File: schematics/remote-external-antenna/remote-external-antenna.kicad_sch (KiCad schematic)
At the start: 0 parts

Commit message: Added eeprom wiring to schematic
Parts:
- added R1, R2: R, symbol Device:R
- added U1: XIAO-ESP32-C6-SMD, Seeed_Studio_XIAO_Series:XIAO-ESP32-C6-SMD, symbol Seeed_Studio_XIAO_Series:XIAO-ESP32-C6-SMD
- added U2: 24LC1025, Package_SO:SOIC-8_3.9x4.9mm_P1.27mm, symbol Memory_EEPROM:24LC1025
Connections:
- new net: R2.2, U1.5 (D4), U2.5 (SDA)
- new net: R1.2, U1.6 (D5), U2.6 (SCL)
- new net +3V3: R1.1, R2.1, U1.12 (3V3_OUT), U2.1 (A0), U2.2 (A1), U2.3 (A2), U2.8 (VCC)
- new net GND: U1.13 (GND), U2.4 (GND), U2.7 (WP)
- no-connect marks 0 -> 11

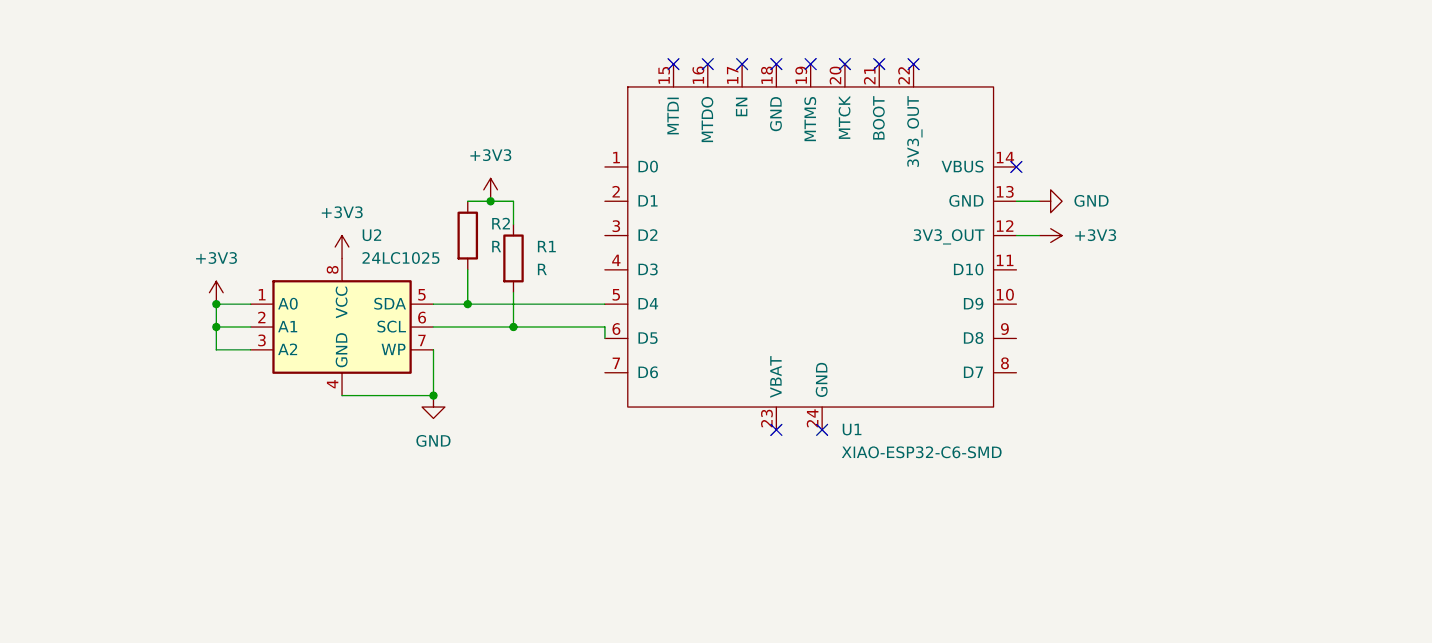
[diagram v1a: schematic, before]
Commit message: expanded schematic with led button and cc1101 module
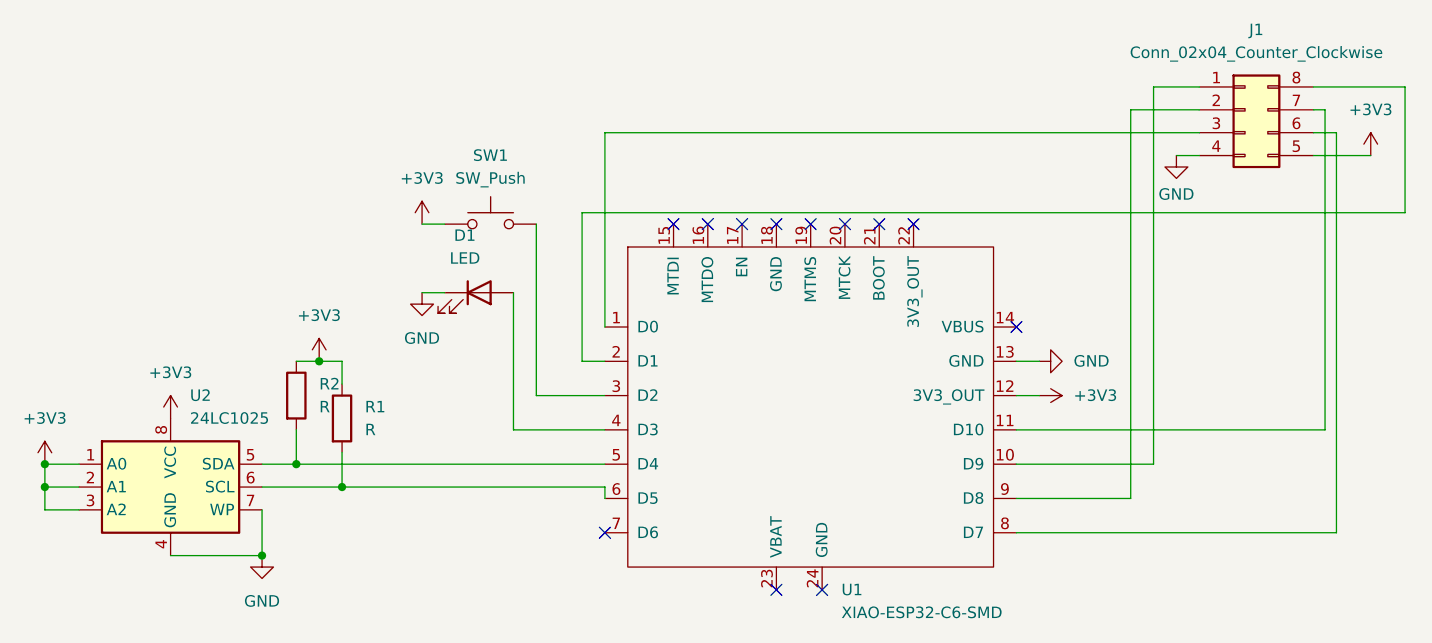
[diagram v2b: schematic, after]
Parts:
- added D1: LED, symbol Device:LED
- added J1: Conn_02x04_Counter_Clockwise, symbol Connector_Generic:Conn_02x04_Counter_Clockwise
- added SW1: SW_Push, symbol Switch:SW_Push
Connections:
- net +3V3: now also J1.5 (Pin_5), SW1.1
- net GND: now also D1.1 (K), J1.4 (Pin_4)
- net at U1.1 (D0): now also J1.3 (Pin_3)
- net at U1.10 (D9): now also J1.1 (Pin_1)
- net at U1.11 (D10): now also J1.7 (Pin_7)
- net at U1.2 (D1): now also J1.8 (Pin_8)
- net at U1.3 (D2): now also SW1.2
- net at U1.4 (D3): now also D1.2 (A)
- net at U1.8 (D7): now also J1.6 (Pin_6)
- net at U1.9 (D8): now also J1.2 (Pin_2)
- no-connect marks 11 -> 12
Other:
- moved on the sheet: R1, R2, U1, U2
